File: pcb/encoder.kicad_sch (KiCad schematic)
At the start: 20 parts, among them J1 GPIO, J2 Foot Switch, J3 X, J4 X', J5 Y, J6 Z

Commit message: assign footprints
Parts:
- C1, C2: footprint (none) -> Capacitor_SMD:C_0603_1608Metric
- C3: footprint (none) -> Capacitor_SMD:C_0805_2012Metric
- J2, J3, J4, J5, J6: footprint (none) -> TerminalBlock_Phoenix:TerminalBlock_Phoenix_PT-1,5-4-5.0-H_1x04_P5.00mm_Horizontal
- R1, R2, R3, R4, R5, R6, R7, R8, R9: footprint (none) -> Resistor_SMD:R_0603_1608Metric
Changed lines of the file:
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@@
 			)
 		)
-		(property "Footprint" ""
+		(property "Footprint" "TerminalBlock_Phoenix:TerminalBlock_Phoenix_PT-1,5-4-5.0-H_1x04_P5.00mm_Horizontal"
 			(at 54.61 177.8 0)
 			(effects
@@
 			)
 		)
-		(property "Footprint" ""
+		(property "Footprint" "Resistor_SMD:R_0603_1608Metric"
 			(at 226.06 135.89 0)
 			(effects
@@
 			)
 		)
-		(property "Footprint" ""
+		(property "Footprint" "Resistor_SMD:R_0603_1608Metric"
 			(at 116.84 157.48 0)
 			(effects
@@
 			)
 		)
-		(property "Footprint" ""
+		(property "Footprint" "TerminalBlock_Phoenix:TerminalBlock_Phoenix_PT-1,5-4-5.0-H_1x04_P5.00mm_Horizontal"
 			(at 81.28 81.28 0)
 			(effects
@@
 			)
 		)
-		(property "Footprint" ""
+		(property "Footprint" "Capacitor_SMD:C_0603_1608Metric"
 			(at 96.52 124.46 0)
 			(effects
@@
 			)
 		)
-		(property "Footprint" ""
+		(property "Footprint" "Resistor_SMD:R_0603_1608Metric"
 			(at 215.9 135.89 0)
 			(effects
@@
 			)
 		)
-		(property "Footprint" ""
+		(property "Footprint" "Resistor_SMD:R_0603_1608Metric"
 			(at 106.68 157.48 0)
 			(effects
@@
 			)
 		)
-		(property "Footprint" ""
+		(property "Footprint" "TerminalBlock_Phoenix:TerminalBlock_Phoenix_PT-1,5-4-5.0-H_1x04_P5.00mm_Horizontal"
 			(at 107.95 177.8 0)
 			(effects
@@
 			)
 		)
-		(property "Footprint" ""
+		(property "Footprint" "Resistor_SMD:R_0603_1608Metric"
 			(at 29.21 157.48 0)
 			(effects
@@
 			)
 		)
-		(property "Footprint" ""
+		(property "Footprint" "Resistor_SMD:R_0603_1608Metric"
 			(at 95.25 74.93 0)
 			(effects
@@
 			)
 		)
-		(property "Footprint" ""
+		(property "Footprint" "TerminalBlock_Phoenix:TerminalBlock_Phoenix_PT-1,5-4-5.0-H_1x04_P5.00mm_Horizontal"
 			(at 163.83 177.8 0)
 			(effects
@@
 			)
 		)
-		(property "Footprint" ""
+		(property "Footprint" "Resistor_SMD:R_0603_1608Metric"
 			(at 19.05 157.48 0)
 			(effects
@@
 			)
 		)
-		(property "Footprint" ""
+		(property "Footprint" "Resistor_SMD:R_0603_1608Metric"
 			(at 142.24 157.48 0)
 			(effects
@@
 			)
 		)
-		(property "Footprint" ""
+		(property "Footprint" "Resistor_SMD:R_0603_1608Metric"
 			(at 132.08 157.48 0)
 			(effects
@@
 			)
 		)
-		(property "Footprint" ""
+		(property "Footprint" "TerminalBlock_Phoenix:TerminalBlock_Phoenix_PT-1,5-4-5.0-H_1x04_P5.00mm_Horizontal"
 			(at 243.84 140.97 0)
 			(effects
@@
 			)
 		)
-		(property "Footprint" ""
+		(property "Footprint" "Capacitor_SMD:C_0805_2012Metric"
 			(at 120.65 27.94 0)
 			(effects
@@
 			)
 		)
-		(property "Footprint" ""
+		(property "Footprint" "Capacitor_SMD:C_0603_1608Metric"
 			(at 208.28 124.46 0)
 			(effects

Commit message: snapshot...working on routing
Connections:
- net +5V: now also J3.4 (Pin_4), J4.4 (Pin_4), J5.4 (Pin_4); no longer J3.1 (Pin_1), J4.1 (Pin_1), J5.1 (Pin_1)
- net GND: now also J3.1 (Pin_1), J4.1 (Pin_1), J5.1 (Pin_1); no longer J3.4 (Pin_4), J4.4 (Pin_4), J5.4 (Pin_4)
- net at LS7466-S1.6 (Bx), R3.2: now also J3.3 (Pin_3); no longer J3.2 (Pin_2)
- net at LS7466-S1.5 (Ax), R2.2: now also J3.2 (Pin_2); no longer J3.3 (Pin_3)
- net at LS7466-S2.11 (Ay), R9.2: now also J6.2 (Pin_2); no longer J6.3 (Pin_3)
- net at LS7466-S1.12 (By), R7.2: now also J4.3 (Pin_3); no longer J4.2 (Pin_2)
- net at LS7466-S1.11 (Ay), R6.2: now also J4.2 (Pin_2); no longer J4.3 (Pin_3)
- net at LS7466-S2.12 (By), R8.2: now also J6.3 (Pin_3); no longer J6.2 (Pin_2)
- net at LS7466-S2.6 (Bx), R5.2: now also J5.3 (Pin_3); no longer J5.2 (Pin_2)
- net at LS7466-S2.5 (Ax), R4.2: now also J5.2 (Pin_2); no longer J5.3 (Pin_3)
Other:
- moved on the sheet: C3, J3, J4, J5, J6

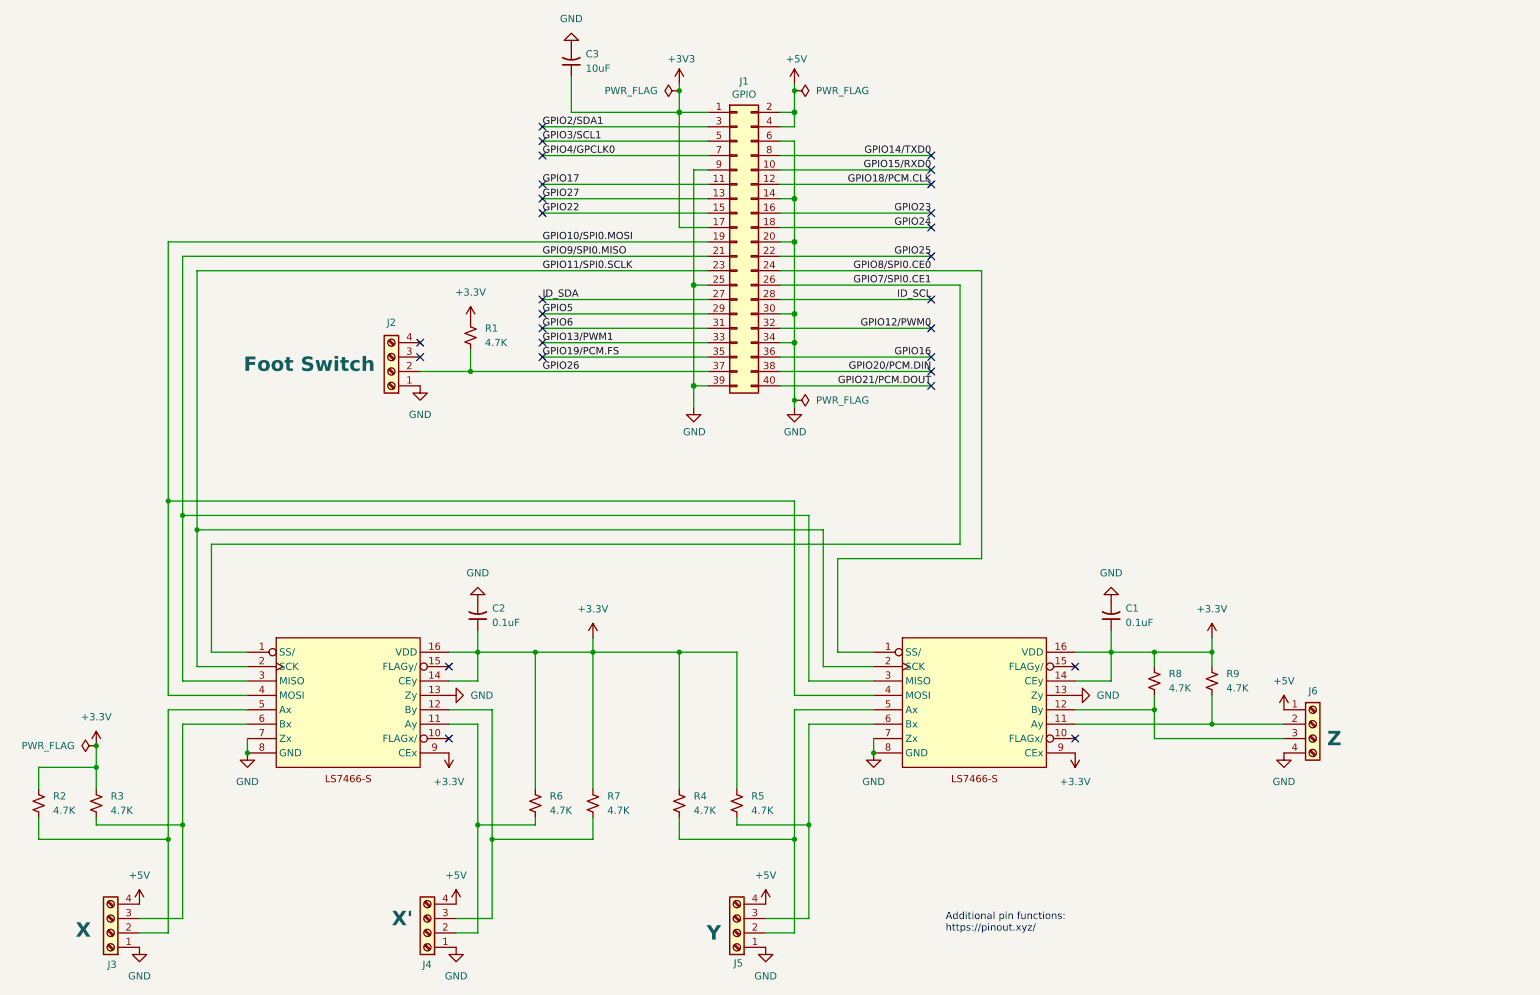
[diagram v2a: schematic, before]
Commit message: route with ls74633 chips
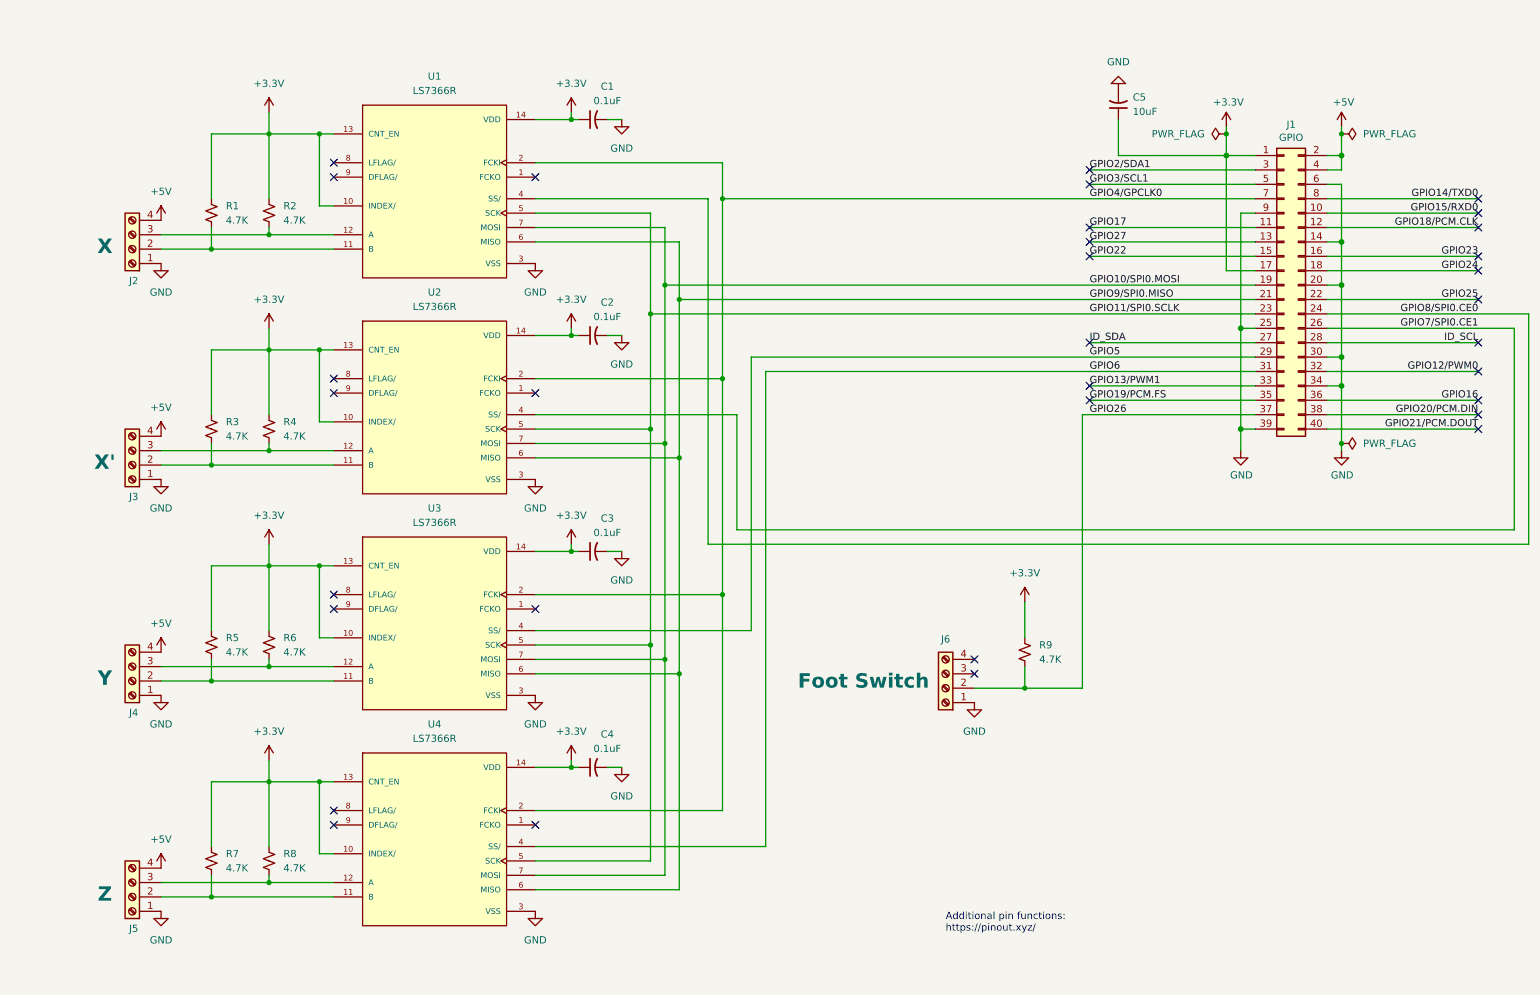
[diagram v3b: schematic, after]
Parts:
- removed J6: Z, TerminalBlock_Phoenix:TerminalBlock_Phoenix_PT-1,5-4-5.0-H_1x04_P5.00mm_Horizontal, symbol Connector:Screw_Terminal_01x04
- removed LS7466-S1, LS7466-S2: ~, Package_SO:SOIC-16_3.9x9.9mm_P1.27mm, symbol LS7466:LS7466-S
- removed R9: 4.7K, Resistor_SMD:R_0603_1608Metric, symbol Device:R_Small_US
- added C3, C4: 0.1uF, Capacitor_SMD:C_0603_1608Metric, symbol Device:C_Small_US
- added J2: X, TerminalBlock_Phoenix:TerminalBlock_Phoenix_PT-1,5-4-5.0-H_1x04_P5.00mm_Horizontal, symbol Connector:Screw_Terminal_01x04
- added R1: 4.7K, Resistor_SMD:R_0603_1608Metric, symbol Device:R_Small_US
- added U1, U2, U3, U4: LS7366R, LS7366R:DIP762W45P254L1917H533Q14, symbol library:LS7366R
- J3: value X -> X'
- J4: value X' -> Y
- J5: value Y -> Z
- renumbered C3 to C5, J2 to J6, R1 to R9
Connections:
- net +3V3 is gone; now on net +3.3V: C5.1, J1.1 (Pin_1), J1.17 (Pin_17)
- net +3.3V: now also C3.1, C4.1, R1.1, U1.10 (INDEX/), U1.13 (CNT_EN), U1.14 (VDD), U2.10 (INDEX/), U2.13 (CNT_EN), U2.14 (VDD), U3.10 (INDEX/), U3.13 (CNT_EN), U3.14 (VDD), U4.10 (INDEX/), U4.13 (CNT_EN), U4.14 (VDD)
- net +5V: now also J2.4 (Pin_4)
- net GND: now also C3.2, C4.2, J2.1 (Pin_1), U1.3 (VSS), U2.3 (VSS), U3.3 (VSS), U4.3 (VSS)
- net GPIO10/SPI0.MOSI: now also U1.7 (MOSI), U2.7 (MOSI), U3.7 (MOSI), U4.7 (MOSI)
- net GPIO11/SPI0.SCLK: now also U1.5 (SCK), U2.5 (SCK), U3.5 (SCK), U4.5 (SCK)
- net GPIO4/GPCLK0: now also U1.2 (FCKI), U2.2 (FCKI), U3.2 (FCKI), U4.2 (FCKI)
- net GPIO5: now also U3.4 (SS/)
- net GPIO6: now also U4.4 (SS/)
- net GPIO7/SPI0.CE1: now also U2.4 (SS/)
- net GPIO8/SPI0.CE0: now also U1.4 (SS/)
- net GPIO9/SPI0.MISO: now also U1.6 (MISO), U2.6 (MISO), U3.6 (MISO), U4.6 (MISO)
- net at R2.2: now also J2.3 (Pin_3), U1.12 (A); no longer J3.2 (Pin_2)
- net at R3.2: now also J3.2 (Pin_2), U2.11 (B); no longer J3.3 (Pin_3)
- net at J4.3 (Pin_3): now also R6.2, U3.12 (A); no longer R7.2
- net at J4.2 (Pin_2): now also R5.2, U3.11 (B); no longer R6.2
- net at R8.2: now also J5.3 (Pin_3), U4.12 (A)
- net at R4.2: now also J3.3 (Pin_3), U2.12 (A); no longer J5.2 (Pin_2)
- new net: J2.2 (Pin_2), R1.2, U1.11 (B)
- new net: J5.2 (Pin_2), R7.2, U4.11 (B)
- no-connect marks 28 -> 33
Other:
- moved on the sheet: C5, J1, J6, R9

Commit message: update BOM
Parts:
- C1, C2, C3, C4: MPN (none) -> GRM188R71E104KA01D; Manufacturer (none) -> Murata
- C5: MPN (none) -> GRM21BR61A106KE19L; Manufacturer (none) -> Murata
- J1, J2, J3, J4, J5, J6, U1, U2, U3, U4: now left out of the parts list
- R1, R2, R3, R4, R5, R6, R7, R8, R9: MPN (none) -> RC0603FR-074K7L; Manufacturer (none) -> Yageo

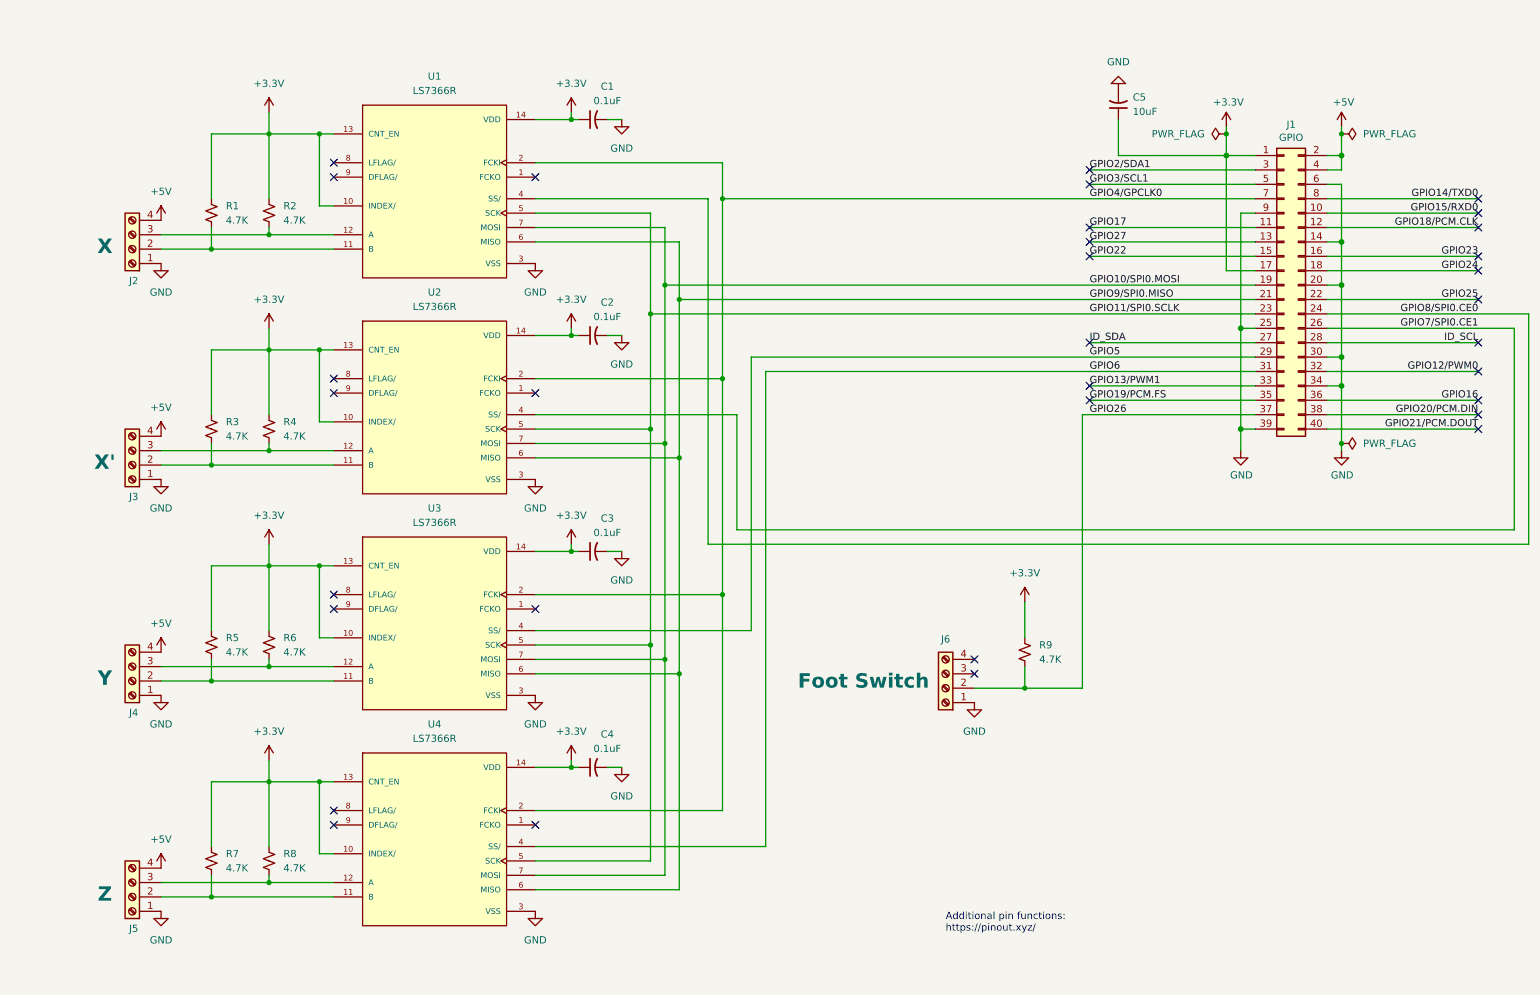
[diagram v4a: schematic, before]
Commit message: move to thru-hole resistors/caps to save costs
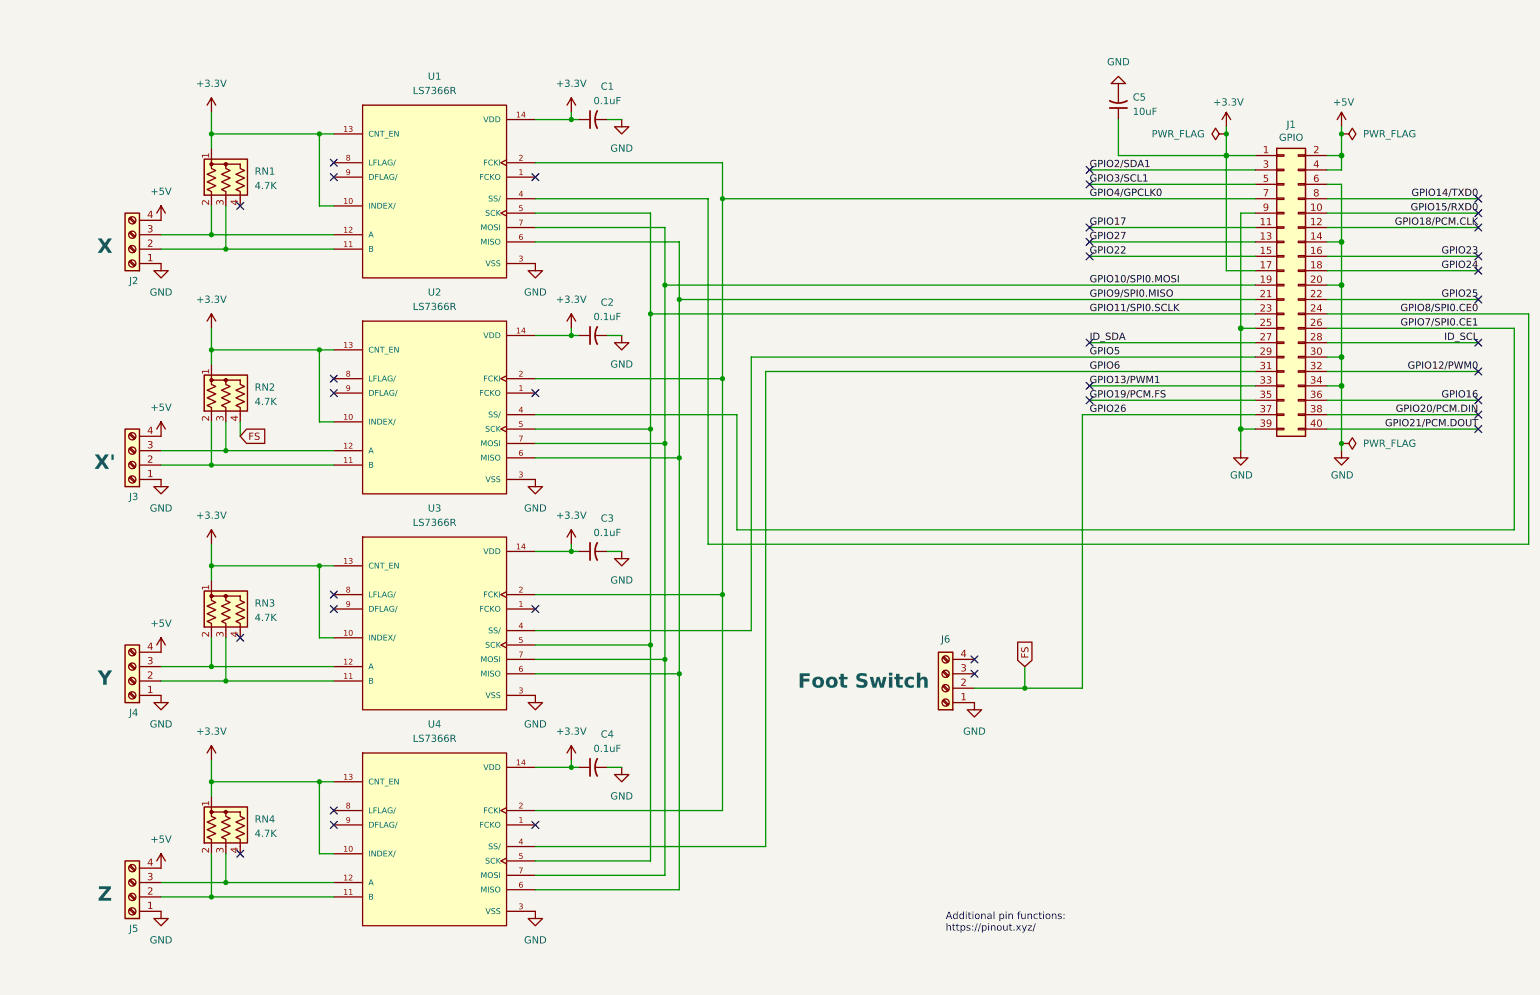
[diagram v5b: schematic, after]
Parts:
- removed R1, R2, R3, R4, R5, R6, R7, R8, R9: 4.7K, Resistor_SMD:R_0603_1608Metric, symbol Device:R_Small_US
- added RN1, RN2, RN3, RN4: 4.7K, Resistor_THT:R_Array_SIP4, symbol Device:R_Network03_US
- C1, C2, C3, C4: footprint Capacitor_SMD:C_0603_1608Metric -> Capacitor_THT:C_Disc_D3.8mm_W2.6mm_P2.50mm; MPN GRM188R71E104KA01D -> C315C104K5R5TA; Manufacturer Murata -> Kemet
- C5: footprint Capacitor_SMD:C_0805_2012Metric -> Capacitor_THT:C_Disc_D5.0mm_W2.5mm_P2.50mm; MPN GRM21BR61A106KE19L -> C322C106K8R5TA; Manufacturer Murata -> Kemet
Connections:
- net +3.3V: now also RN1.1 (common), RN2.1 (common), RN3.1 (common), RN4.1 (common)
- net at J2.3 (Pin_3), U1.12 (A): now also RN1.2 (R1)
- net at J3.2 (Pin_2), U2.11 (B): now also RN2.2 (R1)
- net at J4.2 (Pin_2), U3.11 (B): now also RN3.3 (R2)
- net at J4.3 (Pin_3), U3.12 (A): now also RN3.2 (R1)
- net at J2.2 (Pin_2), U1.11 (B): now also RN1.3 (R2)
- net at J3.3 (Pin_3), U2.12 (A): now also RN2.3 (R2)
- net at J5.2 (Pin_2), U4.11 (B): now also RN4.2 (R1)
- net at J5.3 (Pin_3), U4.12 (A): now also RN4.3 (R2)
- net GPIO26 renamed FS
- net FS: now also RN2.4 (R3)
- no-connect marks 33 -> 36

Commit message: sync hardware.md with BOM from schematic
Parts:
- C1, C2, C3, C4: MPN C315C104K5R5TA -> FA18X8R1E104KNU00; Manufacturer Kemet -> TDK
- C5: MPN C322C106K8R5TA -> FG14X7R1A106KRT00; Manufacturer Kemet -> TDK
- RN1, RN2, RN3, RN4: MPN 77041472P -> 4604X-101-472LF; Manufacturer CTS -> Bourns
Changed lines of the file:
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@@
 			)
 		)
-		(property "MPN" "77041472P"
+		(property "MPN" "4604X-101-472LF"
 			(at 52.07 161.29 0)
 			(effects
@@
 			)
 		)
-		(property "Manufacturer" "CTS"
+		(property "Manufacturer" "Bourns"
 			(at 52.07 161.29 0)
 			(effects
@@
 			)
 		)
-		(property "MPN" "C315C104K5R5TA"
+		(property "MPN" "FA18X8R1E104KNU00"
 			(at 116.84 113.03 90)
 			(effects
@@
 			)
 		)
-		(property "Manufacturer" "Kemet"
+		(property "Manufacturer" "TDK"
 			(at 116.84 113.03 90)
 			(effects
@@
 			)
 		)
-		(property "MPN" "C315C104K5R5TA"
+		(property "MPN" "FA18X8R1E104KNU00"
 			(at 116.84 36.83 90)
 			(effects
@@
 			)
 		)
-		(property "Manufacturer" "Kemet"
+		(property "Manufacturer" "TDK"
 			(at 116.84 36.83 90)
 			(effects
@@
 			)
 		)
-		(property "MPN" "C315C104K5R5TA"
+		(property "MPN" "FA18X8R1E104KNU00"
 			(at 116.84 74.93 90)
 			(effects
@@
 			)
 		)
-		(property "Manufacturer" "Kemet"
+		(property "Manufacturer" "TDK"
 			(at 116.84 74.93 90)
 			(effects
@@
 			)
 		)
-		(property "MPN" "77041472P"
+		(property "MPN" "4604X-101-472LF"
 			(at 52.07 123.19 0)
 			(effects
@@
 			)
 		)
-		(property "Manufacturer" "CTS"
+		(property "Manufacturer" "Bourns"
 			(at 52.07 123.19 0)
 			(effects
@@
 			)
 		)
-		(property "MPN" "C315C104K5R5TA"
+		(property "MPN" "FA18X8R1E104KNU00"
 			(at 116.84 151.13 90)
 			(effects
@@
 			)
 		)
-		(property "Manufacturer" "Kemet"
+		(property "Manufacturer" "TDK"
 			(at 116.84 151.13 90)
 			(effects
@@
 			)
 		)
-		(property "MPN" "77041472P"
+		(property "MPN" "4604X-101-472LF"
 			(at 52.07 85.09 0)
 			(effects
@@
 			)
 		)
-		(property "Manufacturer" "CTS"
+		(property "Manufacturer" "Bourns"
 			(at 52.07 85.09 0)
 			(effects
@@
 			)
 		)
-		(property "MPN" "C322C106K8R5TA"
+		(property "MPN" "FG14X7R1A106KRT00"
 			(at 209.55 34.29 0)
 			(effects
@@
 			)
 		)
-		(property "Manufacturer" "Kemet"
+		(property "Manufacturer" "TDK"
 			(at 209.55 34.29 0)
 			(effects
@@
 			)
 		)
-		(property "MPN" "77041472P"
+		(property "MPN" "4604X-101-472LF"
 			(at 52.07 46.99 0)
 			(effects
@@
 			)
 		)
-		(property "Manufacturer" "CTS"
+		(property "Manufacturer" "Bourns"
 			(at 52.07 46.99 0)
 			(effects
